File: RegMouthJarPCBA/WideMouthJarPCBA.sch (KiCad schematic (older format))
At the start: 39 parts, among them CON1 BARREL_JACK, CON2 BARREL_JACK, CON3 BARREL_JACK, J1 8P8C, U1 LTC2057, U2 LM399A, U3 LTC2057, U4 LTC2057, U5 LTC2057

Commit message: first revision of the LM399 board.
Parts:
- removed C4: 0.1uF, ~, symbol C_CER
- removed CON1, CON2, CON3: BARREL_JACK, ~, symbol BARREL_JACK
- removed D1, D2, D3: 1N4148, ~, symbol DIODE
- removed D4, D5, D6, D7, D8, D9: DIODE, ~, symbol DIODE
- removed J1: 8P8C, ~, symbol 8P8C
- removed R1, R2: 100k, ~, symbol R_0W25_1PCT
- added K1: CONN_3, ~, symbol CONN_3
- added P1, P3, P4, P5, P6, P7: CONN_2, ~, symbol CONN_2
- C1, C2, C3: value 1uF -> 10uF
- C5: value 0.1uF -> 10nF
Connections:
- net labels added: 2.9Vo, 290mVo, 29Vo, 29mVo, Op-, SD, Vz
- net labels removed: 29V, 4.5V
- wire segments 170 -> 119
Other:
- note removed: "(startup)"
- moved on the sheet: C1, C10, C11, C12, C3

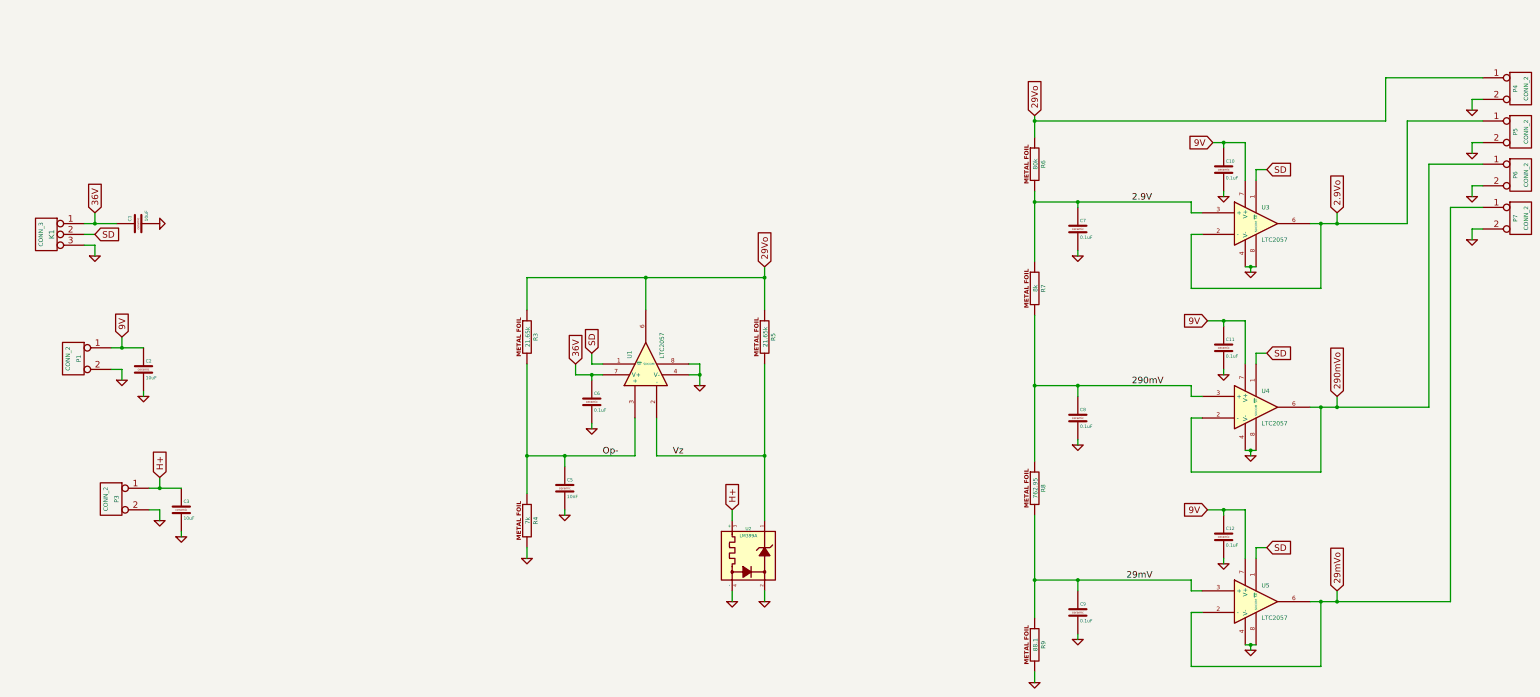
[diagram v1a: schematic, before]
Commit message: implemented guard traces for LM399 reference board.  producing pcb's as v1.
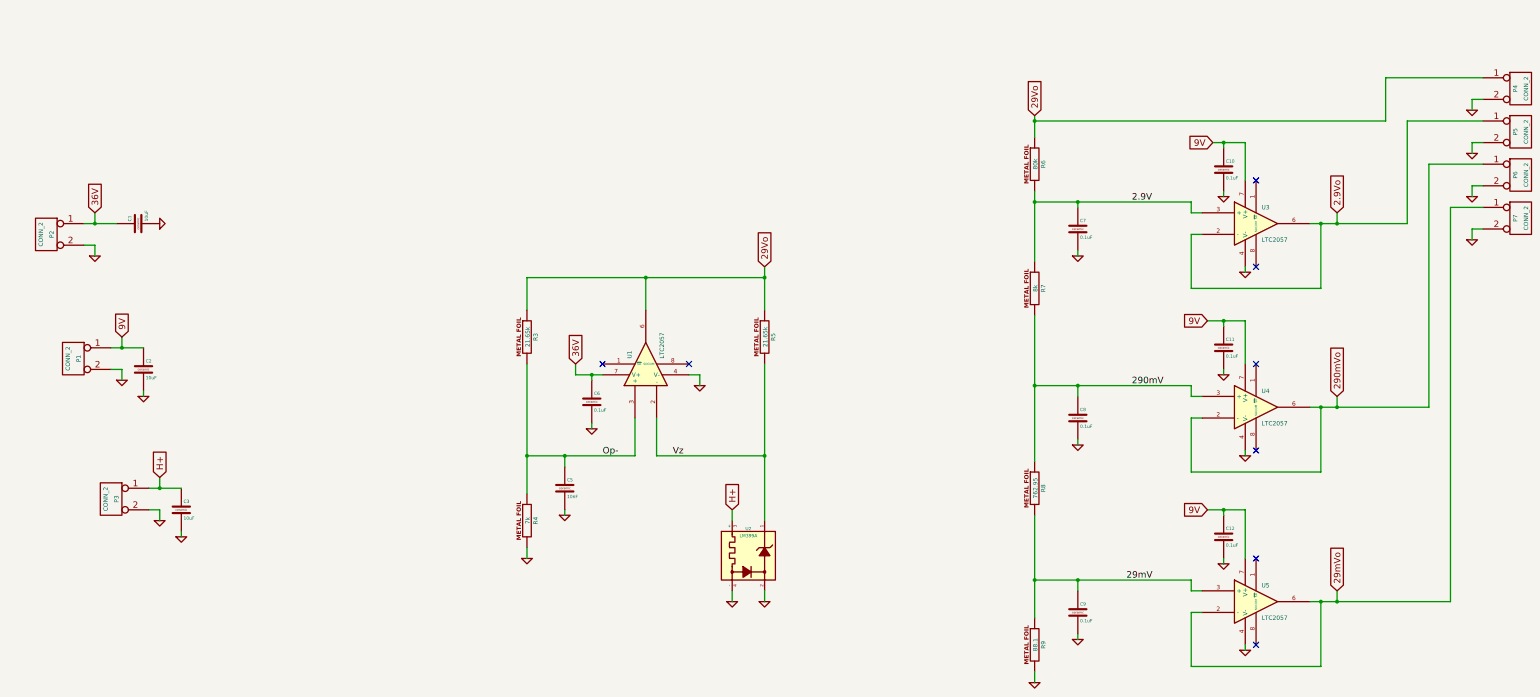
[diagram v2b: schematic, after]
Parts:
- removed K1: CONN_3, ~, symbol CONN_3
- added P2: CONN_2, ~, symbol CONN_2
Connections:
- net 36V: now also P2.1 (P1)
- net GND: now also P2.2 (PM); no longer U1.8 (SDCOM), U3.8 (SDCOM), U4.8 (SDCOM), U5.8 (SDCOM)
- removed net SD: U1.1 (~SD), U3.1 (~SD), U4.1 (~SD), U5.1 (~SD)
- no-connect marks 0 -> 8
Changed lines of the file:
@@
 EESchema Schematic File Version 2
+LIBS:WideMouthJarPCBA-cache
 LIBS:analog_ICs_PL
 LIBS:capacitors_PL
@@
 Text GLabel 2550 4050 1    60   Input ~ 0
 36V
-Text GLabel 7150 5350 1    60   Input ~ 0
-SD
 Text GLabel 8750 4550 1    60   Input ~ 0
 29Vo
@@
 L GND #PWR06
 U 1 1 53ACBFEC
-P 13250 4600
-F 0 "#PWR06" H 13250 4600 30  0001 C CNN
-F 1 "GND" H 13250 4530 30  0001 C CNN
-F 2 "" H 13250 4600 60  0000 C CNN
-F 3 "" H 13250 4600 60  0000 C CNN
-	1    13250 4600
+P 13200 4600
+F 0 "#PWR06" H 13200 4600 30  0001 C CNN
+F 1 "GND" H 13200 4530 30  0001 C CNN
+F 2 "" H 13200 4600 60  0000 C CNN
+F 3 "" H 13200 4600 60  0000 C CNN
+	1    13200 4600
 	1    0    0    -1
 $EndComp
 Text GLabel 12900 3400 0    60   Input ~ 0
 9V
-Text GLabel 13400 3650 2    60   Input ~ 0
-SD
 $Comp
 L LTC2057 U4
@@
 L GND #PWR07
 U 1 1 53ACC51A
-P 13250 6300
-F 0 "#PWR07" H 13250 6300 30  0001 C CNN
-F 1 "GND" H 13250 6230 30  0001 C CNN
-F 2 "" H 13250 6300 60  0000 C CNN
-F 3 "" H 13250 6300 60  0000 C CNN
-	1    13250 6300
+P 13200 6300
+F 0 "#PWR07" H 13200 6300 30  0001 C CNN
+F 1 "GND" H 13200 6230 30  0001 C CNN
+F 2 "" H 13200 6300 60  0000 C CNN
+F 3 "" H 13200 6300 60  0000 C CNN
+	1    13200 6300
 	1    0    0    -1
 $EndComp
 Text GLabel 12850 5050 0    60   Input ~ 0
 9V
-Text GLabel 13400 5350 2    60   Input ~ 0
-SD
 $Comp
 L LTC2057 U5
@@
 L GND #PWR08
 U 1 1 53ACC547
-P 13250 8100
-F 0 "#PWR08" H 13250 8100 30  0001 C CNN
-F 1 "GND" H 13250 8030 30  0001 C CNN
-F 2 "" H 13250 8100 60  0000 C CNN
-F 3 "" H 13250 8100 60  0000 C CNN
-	1    13250 8100
+P 13200 8100
+F 0 "#PWR08" H 13200 8100 30  0001 C CNN
+F 1 "GND" H 13200 8030 30  0001 C CNN
+F 2 "" H 13200 8100 60  0000 C CNN
+F 3 "" H 13200 8100 60  0000 C CNN
+	1    13200 8100
 	1    0    0    -1
 $EndComp
 Text GLabel 12850 6800 0    60   Input ~ 0
 9V
-Text GLabel 13400 7150 2    60   Input ~ 0
-SD
 $Comp
 L GND #PWR09
@@
 Connection ~ 8750 6300
 Wire Wire Line
-	8050 5450 8150 5450
-Wire Wire Line
-	8150 5450 8150 5650
-Wire Wire Line
 	8050 5550 8150 5550
-Connection ~ 8150 5550
 Wire Wire Line
 	7000 5550 7250 5550
@@
 Wire Wire Line
 	2550 4150 2550 4050
-Wire Wire Line
-	7150 5350 7150 5450
-Wire Wire Line
-	7150 5450 7250 5450
 Connection ~ 8750 4650
 Wire Wire Line
@@
 	7000 5550 7000 5450
 Wire Wire Line
-	13400 3650 13300 3650
-Wire Wire Line
-	13300 3650 13300 3750
-Wire Wire Line
 	12800 4250 12700 4250
 Wire Wire Line
@@
 	13800 4150 14700 4150
 Wire Wire Line
-	13200 4550 13300 4550
-Wire Wire Line
-	13250 4550 13250 4600
-Connection ~ 13250 4550
-Wire Wire Line
 	12900 3400 13200 3400
 Wire Wire Line
@@
 	12700 3950 11250 3950
 Wire Wire Line
-	13400 5350 13300 5350
-Wire Wire Line
-	13300 5350 13300 5450
-Wire Wire Line
 	12800 5950 12700 5950
 Wire Wire Line
@@
 	13800 5850 14900 5850
 Wire Wire Line
-	13200 6250 13300 6250
-Wire Wire Line
-	13250 6250 13250 6300
-Connection ~ 13250 6250
-Wire Wire Line
 	12850 5050 13200 5050
 Wire Wire Line
@@
 	12700 5650 11250 5650
 Wire Wire Line
-	13400 7150 13300 7150
-Wire Wire Line
-	13300 7150 13300 7250
-Wire Wire Line
 	12800 7750 12700 7750
 Wire Wire Line
@@
 Wire Wire Line
 	13800 7650 15100 7650
-Wire Wire Line
-	13200 8050 13300 8050
-Wire Wire Line
-	13250 8050 13250 8100
-Connection ~ 13250 8050
 Wire Wire Line
 	12850 6800 13200 6800
@@
 Wire Wire Line
 	14700 3200 15400 3200
-$Comp
-L CONN_3 K1
-U 1 1 53AFB46B
-P 2100 4250
-F 0 "K1" V 2050 4250 50  0000 C CNN
-F 1 "CONN_3" V 2150 4250 40  0000 C CNN
-F 2 "~" H 2100 4250 60  0000 C CNN
-F 3 "~" H 2100 4250 60  0000 C CNN
-	1    2100 4250
-	-1   0    0    -1
-$EndComp
-Text GLabel 2550 4250 2    60   Input ~ 0
-SD
-Wire Wire Line
-	2450 4250 2550 4250
 Text Label 7250 6300 0    60   ~ 0
 Op-
@@
 Wire Wire Line
 	2800 5500 2800 5600
+$Comp
+L CONN_2 P2
+U 1 1 53B06599
+P 2100 4250
+F 0 "P2" V 2050 4250 40  0000 C CNN
+F 1 "CONN_2" V 2150 4250 40  0000 C CNN
+F 2 "~" H 2100 4250 60  0000 C CNN
+F 3 "~" H 2100 4250 60  0000 C CNN
+	1    2100 4250
+	-1   0    0    -1
+$EndComp
+NoConn ~ 7250 5450
+NoConn ~ 8050 5450
+Wire Wire Line
+	8150 5550 8150 5650
+Wire Wire Line
+	13200 4550 13200 4600
+NoConn ~ 13300 4550
+NoConn ~ 13300 3750
+NoConn ~ 13300 5450
+NoConn ~ 13300 7250
+NoConn ~ 13300 8050
+Wire Wire Line
+	13200 8050 13200 8100
+Wire Wire Line
+	13200 6250 13200 6300
+NoConn ~ 13300 6250
 $EndSCHEMATC

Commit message: substituting 10-pin LTC2057's.
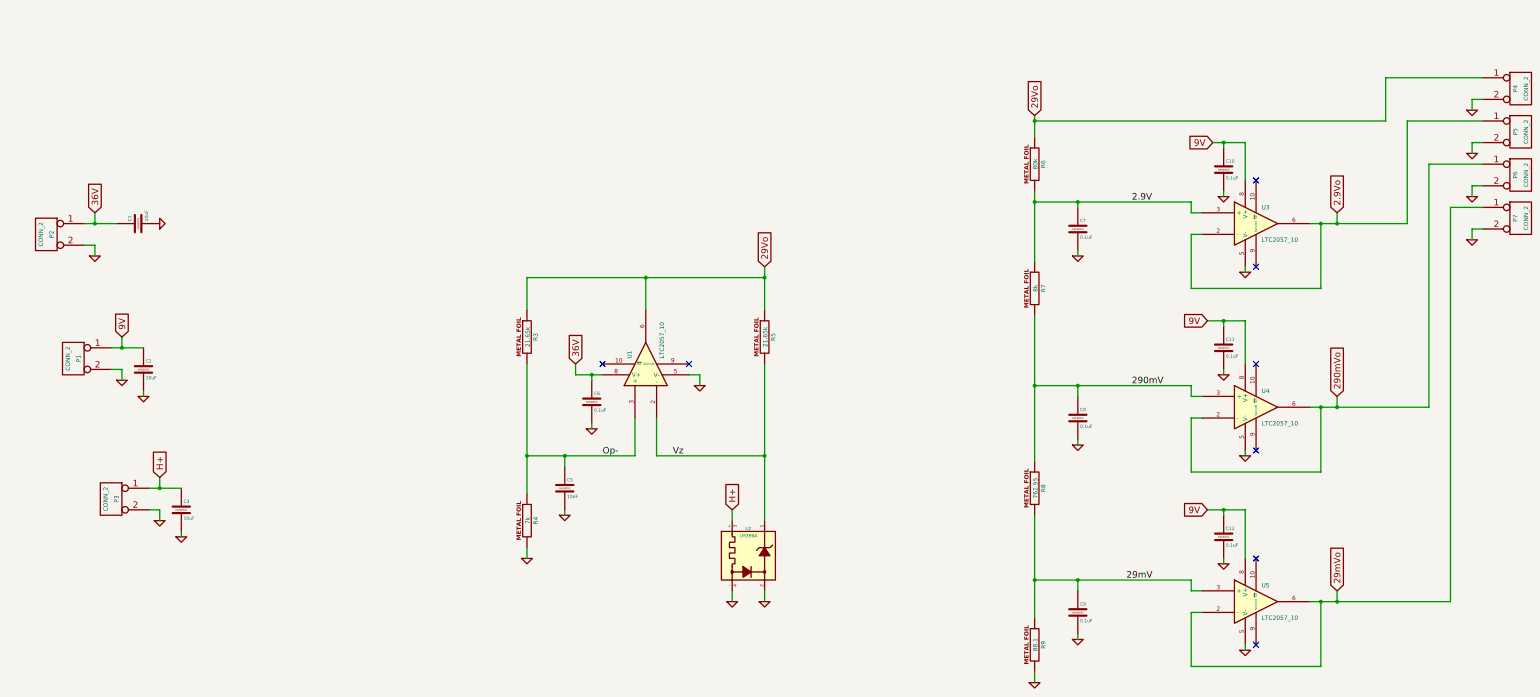
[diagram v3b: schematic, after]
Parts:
- removed U1, U3, U4, U5: LTC2057, ~, symbol LTC2057
- added U1, U3, U4, U5: LTC2057_10, ~, symbol LTC2057_10
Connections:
- net 2.9V: now also U3.3 (+)
- net 2.9Vo: now also U3.2 (-), U3.6
- net 290mV: now also U4.3 (+)
- net 290mVo: now also U4.2 (-), U4.6
- net 29Vo: now also U1.6
- net 29mV: now also U5.3 (+)
- net 29mVo: now also U5.2 (-), U5.6
- net 36V: now also U1.8 (V+)
- net 9V: now also U3.8 (V+), U4.8 (V+), U5.8 (V+)
- net GND: now also U1.5 (V-), U3.5 (V-), U4.5 (V-), U5.5 (V-)
- net Op-: now also U1.3 (+)
- net Vz: now also U1.2 (-)
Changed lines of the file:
@@
 Sheet 1 1
 Title ""
-Date "29 jun 2014"
+Date "15 jul 2014"
 Rev ""
 Comp ""
@@
 $EndComp
 $Comp
-L LTC2057 U1
-U 1 1 53ACBB19
-P 7650 5450
-F 0 "U1" H 7700 5600 40  0000 L CNN
-F 1 "LTC2057" H 7700 5300 40  0000 L CNN
-F 2 "~" H 7650 5450 60  0000 C CNN
-F 3 "~" H 7650 5450 60  0000 C CNN
-	1    7650 5450
-	0    -1   -1   0
-$EndComp
-$Comp
 L R_FOIL R3
 U 1 1 53ACBB97
@@
 29Vo
 $Comp
-L LTC2057 U3
-U 1 1 53ACBFE6
-P 13300 4150
-F 0 "U3" H 13350 4300 40  0000 L CNN
-F 1 "LTC2057" H 13350 4000 40  0000 L CNN
-F 2 "~" H 13300 4150 60  0000 C CNN
-F 3 "~" H 13300 4150 60  0000 C CNN
-	1    13300 4150
-	1    0    0    -1
-$EndComp
-$Comp
 L GND #PWR06
 U 1 1 53ACBFEC
@@
 9V
 $Comp
-L LTC2057 U4
-U 1 1 53ACC514
-P 13300 5850
-F 0 "U4" H 13350 6000 40  0000 L CNN
-F 1 "LTC2057" H 13350 5700 40  0000 L CNN
-F 2 "~" H 13300 5850 60  0000 C CNN
-F 3 "~" H 13300 5850 60  0000 C CNN
-	1    13300 5850
-	1    0    0    -1
-$EndComp
-$Comp
 L GND #PWR07
 U 1 1 53ACC51A
@@
 Text GLabel 12850 5050 0    60   Input ~ 0
 9V
-$Comp
-L LTC2057 U5
-U 1 1 53ACC541
-P 13300 7650
-F 0 "U5" H 13350 7800 40  0000 L CNN
-F 1 "LTC2057" H 13350 7500 40  0000 L CNN
-F 2 "~" H 13300 7650 60  0000 C CNN
-F 3 "~" H 13300 7650 60  0000 C CNN
-	1    13300 7650
-	1    0    0    -1
-$EndComp
 $Comp
 L GND #PWR08
@@
 	13200 6250 13200 6300
 NoConn ~ 13300 6250
+$Comp
+L LTC2057_10 U1
+U 1 1 53C47511
+P 7650 5450
+F 0 "U1" H 7700 5600 40  0000 L CNN
+F 1 "LTC2057_10" H 7700 5300 40  0000 L CNN
+F 2 "~" H 7650 5450 60  0000 C CNN
+F 3 "~" H 7650 5450 60  0000 C CNN
+	1    7650 5450
+	0    -1   -1   0
+$EndComp
+$Comp
+L LTC2057_10 U3
+U 1 1 53C47520
+P 13300 4150
+F 0 "U3" H 13350 4300 40  0000 L CNN
+F 1 "LTC2057_10" H 13350 4000 40  0000 L CNN
+F 2 "~" H 13300 4150 60  0000 C CNN
+F 3 "~" H 13300 4150 60  0000 C CNN
+	1    13300 4150
+	1    0    0    -1
+$EndComp
+$Comp
+L LTC2057_10 U4
+U 1 1 53C4752F
+P 13300 5850
+F 0 "U4" H 13350 6000 40  0000 L CNN
+F 1 "LTC2057_10" H 13350 5700 40  0000 L CNN
+F 2 "~" H 13300 5850 60  0000 C CNN
+F 3 "~" H 13300 5850 60  0000 C CNN
+	1    13300 5850
+	1    0    0    -1
+$EndComp
+$Comp
+L LTC2057_10 U5
+U 1 1 53C4753E
+P 13300 7650
+F 0 "U5" H 13350 7800 40  0000 L CNN
+F 1 "LTC2057_10" H 13350 7500 40  0000 L CNN
+F 2 "~" H 13300 7650 60  0000 C CNN
+F 3 "~" H 13300 7650 60  0000 C CNN
+	1    13300 7650
+	1    0    0    -1
+$EndComp
 $EndSCHEMATC
